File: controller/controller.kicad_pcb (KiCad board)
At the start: 2 copper layers, 74 x 50 mm, 0 parts

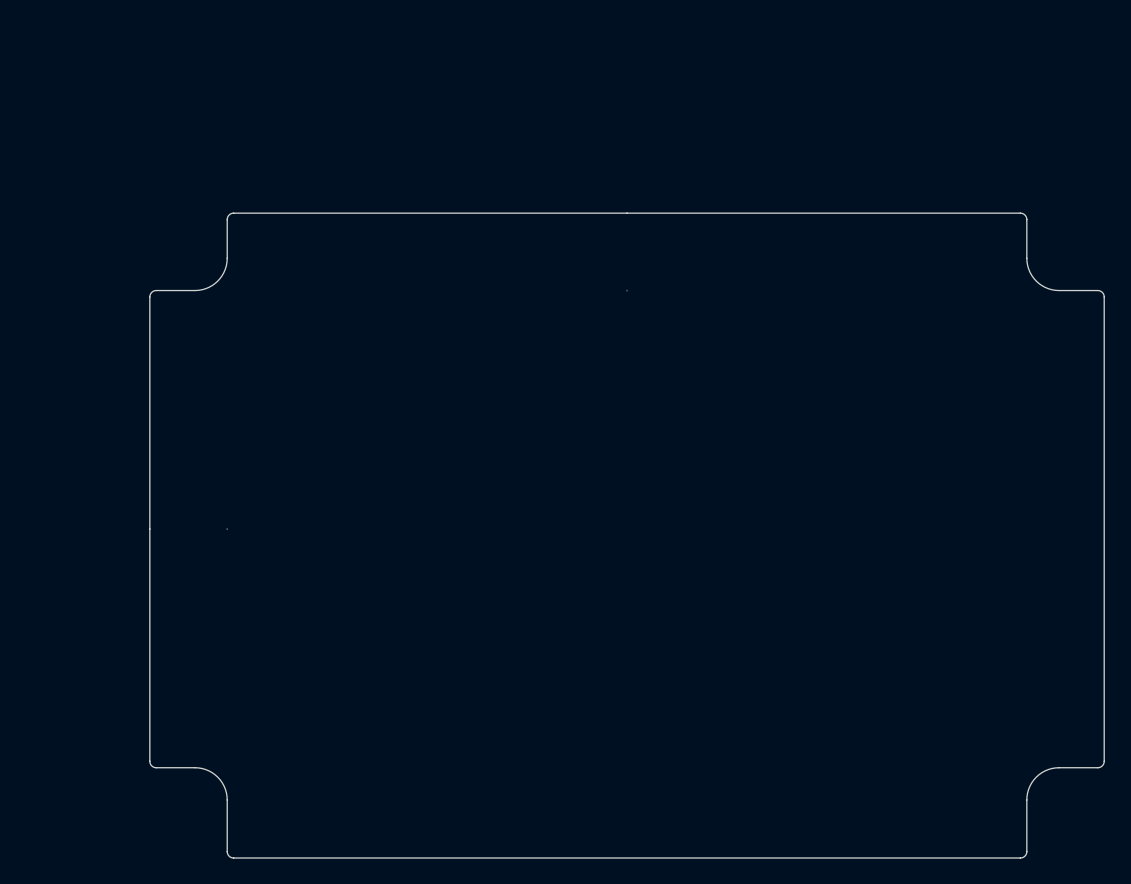
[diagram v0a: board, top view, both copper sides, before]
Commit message: Add footprint for project case PCB
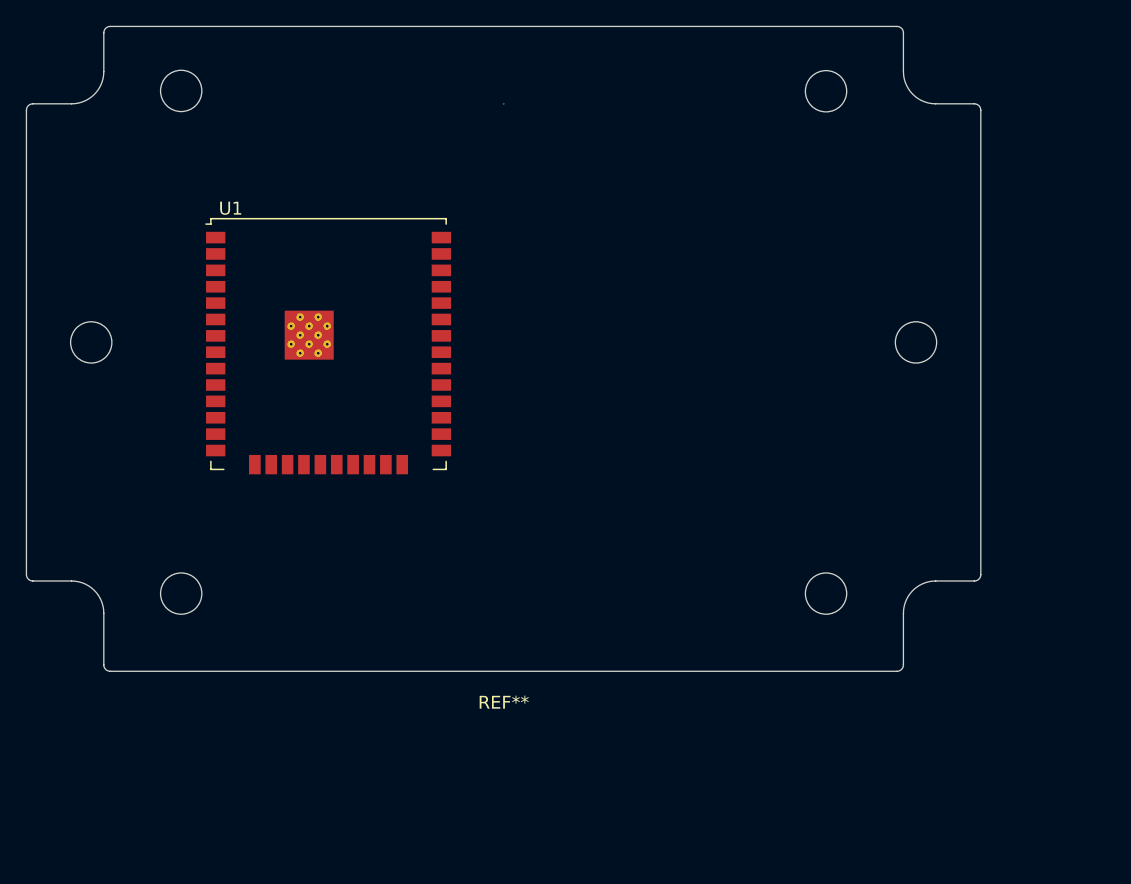
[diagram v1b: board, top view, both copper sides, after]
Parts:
- added REF**: ProjectCase-Small, Controller:ProjectCase-Small, F.Cu at (138.2, 88.9)
- added U1: ESP32-WROOM-32U, RF_Module:ESP32-WROOM-32U, F.Cu at (124.6, 89.0)
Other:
- outline, holes or cut-outs redrawn
